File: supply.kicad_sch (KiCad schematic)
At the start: 118 parts, among them J12 Molex_Nano-Fit_1x2_SMD_105430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, Q11 PJE138K, Q13 BCM857BS-7-F, Q14 BCM857BS-7-F, Q15 SSM3J332R, Q16 SSM3J332R, Q18 SSM3J332R, Q5 PJE138K, Q6 SSM3J332R, Q7 PJE138K, Q8 PJE138K, SW1 SW_SPDT_PCM12SMTR, U1 SIC431AED-T1-GE3, U29 LM73100, U37 74LVC2G14_SOT457, U38 74LVC1G175_SOT457, U40 SIC431AED-T1-GE3, U41 NCP730BMT330_WSON, U42 TPS7A0518P_SOT23-5, U48 LM73100

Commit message: Init commit
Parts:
- C102, C118, C119, C121, C124, C125, C157, C50, C6: LCSC Part # (none) -> C85960
- C103, C120, C126, C127, C128, C129, C153, C154: LCSC Part # (none) -> C2762594
- C116, C117, C137, C83: LCSC Part # (none) -> C105884
- C122, C151, C152, C5: LCSC Part # (none) -> C602037
- C123, C142, C93: LCSC Part # (none) -> C2182694
- C134: LCSC Part # (none) -> C2168289
- C150: LCSC Part # (none) -> C3898487
- C155, C156: LCSC Part # (none) -> C5846150
- C160: LCSC Part # (none) -> C76947
- C161: LCSC Part # (none) -> C2168471
- D28, D29: LCSC Part # (none) -> C1973663
- D30, D31, D32, D33: LCSC Part # (none) -> C41364466
- D36, D37: LCSC Part # (none) -> C145179
- D53: LCSC Part # (none) -> C125093
- D60, D61: LCSC Part # (none) -> C5182093
- J12: LCSC Part # (none) -> C7436819
- L1: LCSC Part # (none) -> C2049215
- L4: LCSC Part # (none) -> C2047688
- Q11, Q5, Q7, Q8: LCSC Part # (none) -> C391643
- Q13, Q14: LCSC Part # (none) -> C105896
- Q15, Q16, Q18, Q6: LCSC Part # (none) -> C146367
- R159, R173, R176, R237, R239, R240: LCSC Part # (none) -> C2085386
- R164, R165: LCSC Part # (none) -> C2076851
- R169: LCSC Part # (none) -> C19946434
- R172, R175, R178, R182, R252, R253: LCSC Part # (none) -> C253507
- R177: LCSC Part # (none) -> C2085419
- R181, R188, R238, R250, R251, R254, R255, R259, R269, R275: LCSC Part # (none) -> C202396
- R183, R260, R264, R268: LCSC Part # (none) -> C242160
- R236: LCSC Part # (none) -> C19946422
- R249: LCSC Part # (none) -> C2077080
- R256: LCSC Part # (none) -> C202394
- R257, R258, R261: LCSC Part # (none) -> C2077217
- R263: LCSC Part # (none) -> C2077214
- R272, R274: LCSC Part # (none) -> C2085488
- R273, R276: LCSC Part # (none) -> C512908
- S4, S5: LCSC Part # (none) -> C221676
- SW1: LCSC Part # (none) -> C221841
- U1, U40: LCSC Part # (none) -> C2071422
- U29, U48: LCSC Part # (none) -> C3210761
- U37: LCSC Part # (none) -> C426708
- U38: LCSC Part # (none) -> C548290
- U41: LCSC Part # (none) -> C892821
- U42: LCSC Part # (none) -> C3752282

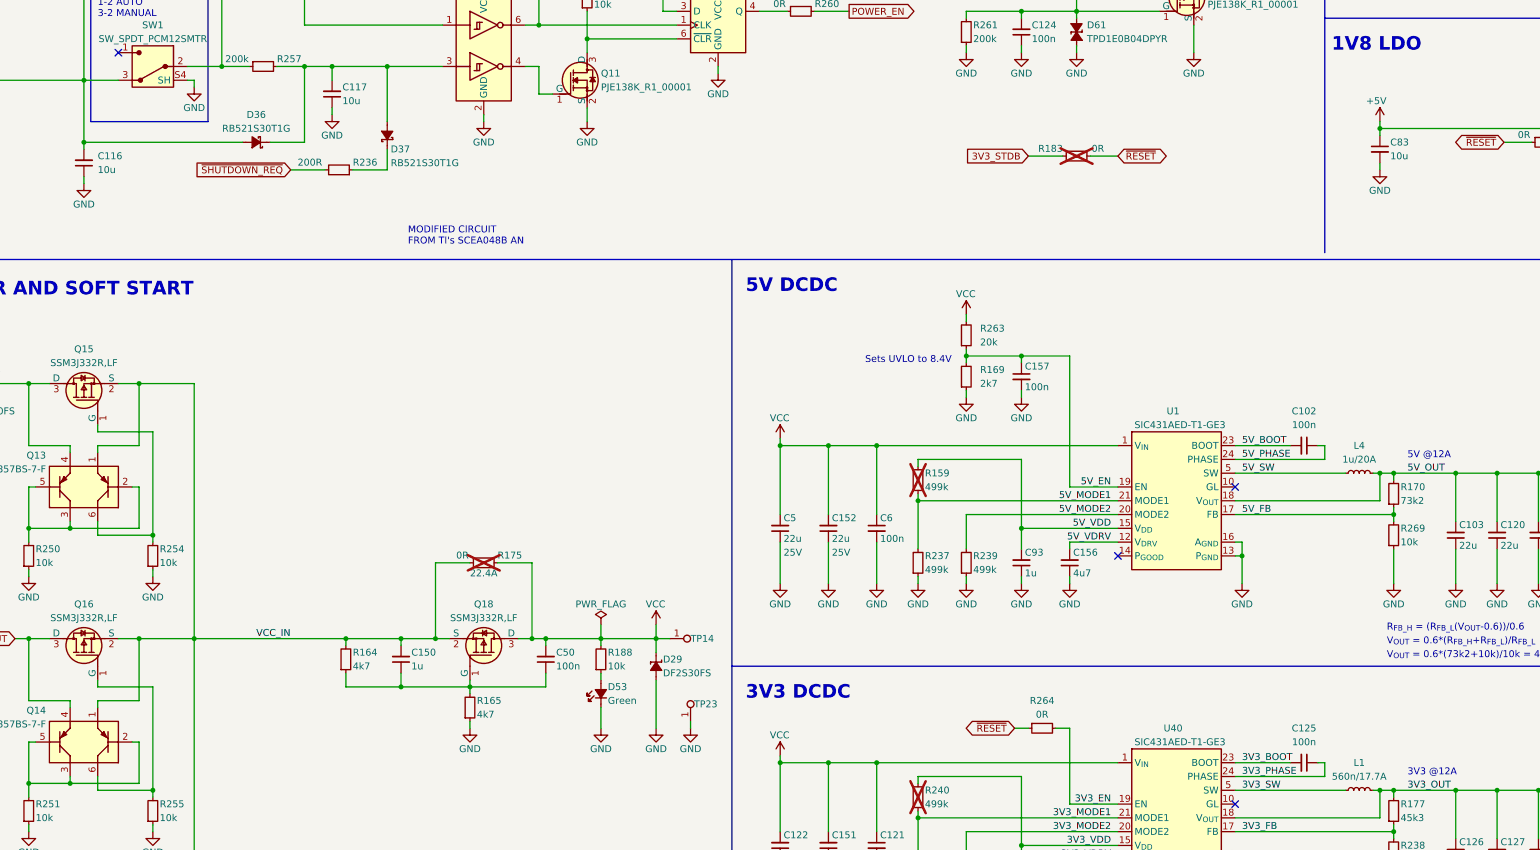
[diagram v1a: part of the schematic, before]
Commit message: Add field Digikey Part Number. Add Chinese substitute components
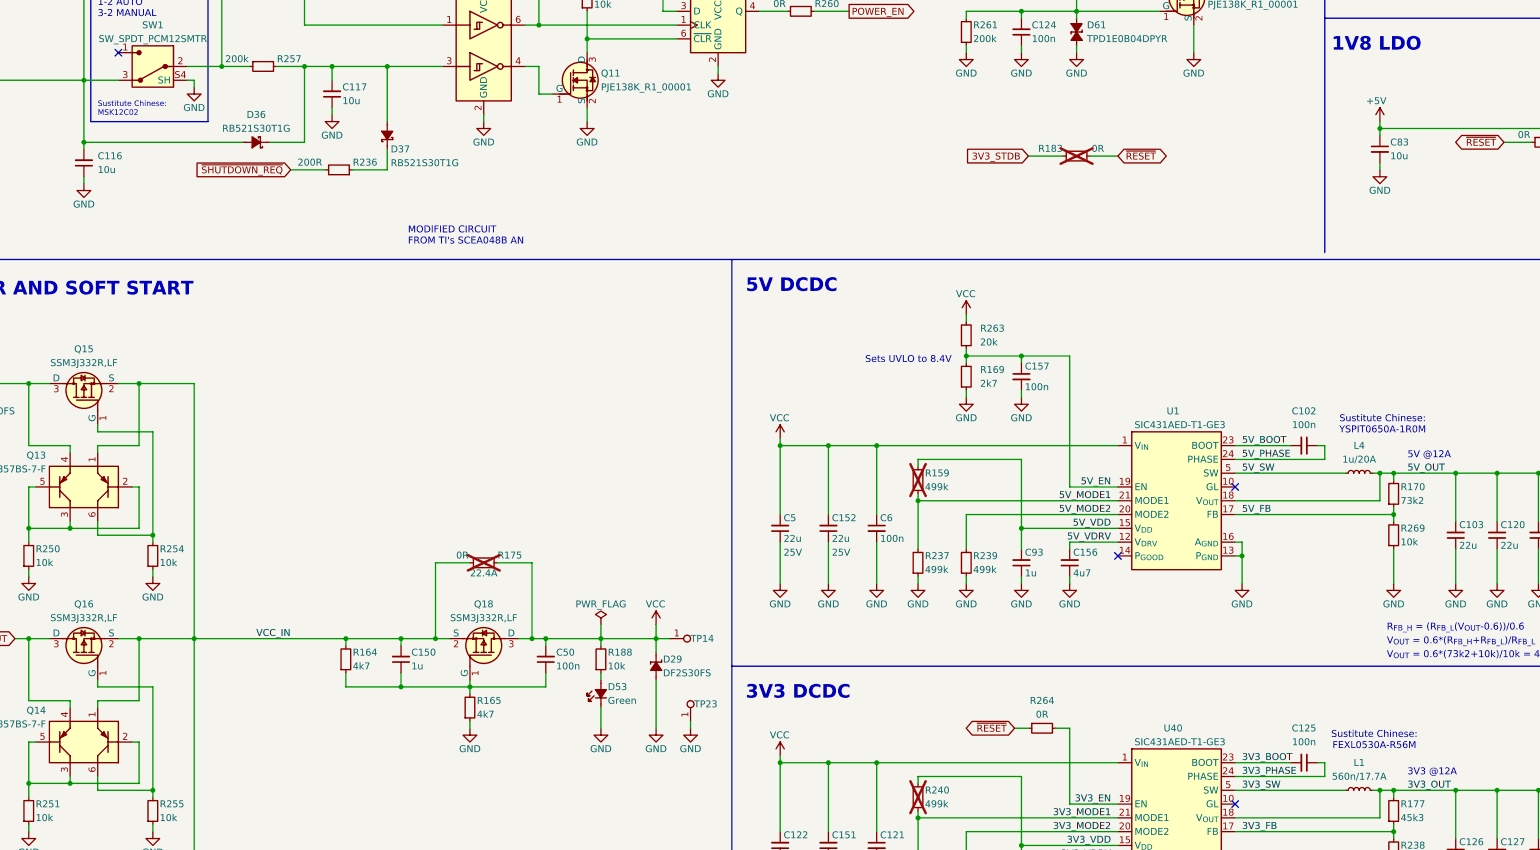
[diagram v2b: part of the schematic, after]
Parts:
- C102, C118, C119, C121, C124, C125, C157, C50, C6: Digikey Part # (none) -> 490-10697-1-ND
- C116, C117, C137, C83: Alternative MPN (none) -> CL05A106MQ5NUNC; Digikey Part # (none) -> 311-1729-1-ND
- C122, C151, C152, C5: Digikey Part # (none) -> 1276-CL21A226MAYNNNECT-ND
- C123, C142, C93: Alternative MPN (none) -> CL05A105KA5NQNC; Digikey Part # (none) -> 445-7368-1-ND
- C134: Alternative MPN (none) -> CL10A106MA8NRNC; Digikey Part # (none) -> 445-9015-1-ND
- C150: Alternative MPN (none) -> CL05A105KA5NQNC; Digikey Part # (none) -> 490-GRM155R61E105KE11JCT-ND
- C155, C156: Digikey Part # (none) -> 490-GRM155C61E475ME15JCT-ND
- C160: Digikey Part # (none) -> 490-3244-1-ND
- C161: Digikey Part # (none) -> 399-C0402C102J4RACTUCT-ND
- D28, D29: Digikey Part # (none) -> DF2S30FSL3MCT-ND
- D30, D31, D32, D33: Digikey Part # (none) -> ESD9X5.0ST5GOSCT-ND
- D36, D37: Digikey Part # (none) -> RB521S30T1GOSCT-ND
- D53: Alternative MPN (none) -> LTST-C190KRKT; Digikey Part # (none) -> 160-1183-1-ND
- D60, D61: Digikey Part # (none) -> 296-47864-1-ND
- J12: Digikey Part # (none) -> WM26097CT-ND
- L1: Digikey Part # (none) -> SRP5030CA-R56MCT-ND
- L4: Digikey Part # (none) -> SRP6050CA-1R0MCT-ND
- Q11, Q5, Q7, Q8: Digikey Part # (none) -> 3757-PJE138K_R1_00001CT-ND
- Q13, Q14: Digikey Part # (none) -> BCM857BS-7-FDICT-ND
- Q15, Q16, Q18, Q6: Digikey Part # (none) -> SSM3J332RLFCT-ND
- R159, R173, R176, R237, R239, R240: Digikey Part # (none) -> CR0402-FX-4993GLFCT-ND
- R164, R165: Digikey Part # (none) -> CR0402-FX-4701GLFCT-ND
- R169: Digikey Part # (none) -> CR0402-FX-2701GLFCT-ND
- R170: Digikey Part # (none) -> 118-CR0402-FX-7322GLFCT-ND
- R172, R175, R178, R182, R252, R253: Digikey Part # (none) -> 846-PMR03EZPJ000CT-ND
- R177: Digikey Part # (none) -> CR0402-FX-4532GLFCT-ND
- R181, R188, R238, R250, R251, R254, R255, R259, R269, R275: Digikey Part # (none) -> CR0402-FX-1002GLFCT-ND
- R183, R260, R264, R268: Digikey Part # (none) -> P0.0JCT-ND
- R236: Digikey Part # (none) -> CR0402-FX-2000GLFCT-ND
- R249: Digikey Part # (none) -> CR0402-FX-1003GLFCT-ND
- R256: Digikey Part # (none) -> CR0402-FX-1001GLFCT-ND
- R257, R258, R261: Digikey Part # (none) -> CR0402-FX-2003GLFCT-ND
- R263: Digikey Part # (none) -> CR0402-FX-2002GLFCT-ND
- R272, R274: Digikey Part # (none) -> CR0402-FX-4703GLFCT-ND
- R273, R276: Digikey Part # (none) -> CR0603-J/-000ELFCT-ND
- S4, S5: Digikey Part # (none) -> CKN10243CT-ND
- SW1: Digikey Part # (none) -> 401-2016-1-ND
- U1, U40: Digikey Part # (none) -> SIC431AED-T1-GE3CT-ND
- U29, U48: Digikey Part # (none) -> 296-LM73100RPWRCT-ND
- U37: Digikey Part # (none) -> 1727-6088-1-ND
- U38: Digikey Part # (none) -> 1727-6068-1-ND
- U41: Digikey Part # (none) -> 488-NCP730BMT330TBGCT-ND
- U42: Digikey Part # (none) -> 296-50251-1-ND
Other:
- note added: "Sustitute Chinese: FEXL0530A-R56M"
- note added: "Sustitute Chinese: MSK12C02"
- note added: "Sustitute Chinese: YSPIT0650A-1R0M"
